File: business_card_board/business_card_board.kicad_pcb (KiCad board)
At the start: 2 copper layers, 23 parts, among them J1 PICKit3_Programmer, SW1 SW_Push, SW2 SW_Push, U1 PIC12F1822

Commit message: layout almost done
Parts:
- J1: moved to B.Cu
- moved 128 72.2 mm to (67.0, 98.0), turned to 270 degrees
- moved D10 63.2 mm to (99.1, 90.9), turned to 180 degrees
- moved D9 62.5 mm to (99.2, 85.6), turned to 180 degrees
- moved R5 61.5 mm to (101.7, 78.3), turned to 90 degrees
- moved 64 60.9 mm to (73.0, 98.0), turned to 90 degrees
- moved R7 60.3 mm to (93.5, 85.6)
- moved R8 60.1 mm to (93.4, 90.9), turned to 180 degrees
- moved 32 49.7 mm to (79.0, 98.0), turned to 270 degrees
- moved R4 49.4 mm to (105.2, 78.3)
- moved U1 47.6 mm to (107.8, 70.7), turned to 180 degrees
- moved R3 43.3 mm to (108.6, 78.3)
- moved R6 43.2 mm to (112.0, 78.3)
- moved C1 39.4 mm to (111.9, 70.9), turned to 270 degrees
- moved R2 38.4 mm to (102.3, 69.2), turned to 0 degrees
- moved 16 38.4 mm to (85.0, 98.0), turned to 90 degrees
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- renumbered SW2 to ->, D1 to 1, D8 to 128, D5 to 16, D2 to 2, D6 to 32, D3 to 4, D7 to 64, D4 to 8, SW1 to <-
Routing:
- net VPP/~MCLR: track 0.00 -> 93.1 mm, vias 0 -> 1
- net Net-(D1-Pad1): track 0.00 -> 74.2 mm
- net Net-(D5-Pad1): track 0.00 -> 68.5 mm
- net Net-(R1-Pad2): track 0.00 -> 61.5 mm
- net Net-(D3-Pad1): track 0.00 -> 48.2 mm
- net Net-(D1-Pad2): track 0.00 -> 44.9 mm
- net ICSPCLK: track 0.00 -> 21.6 mm, vias 0 -> 1
- net ICSPDAT: track 0.00 -> 20.4 mm, vias 0 -> 1
- net RA5: track 0.00 -> 15.4 mm
- net Net-(R5-Pad2): track 0.00 -> 6.18 mm
- net GND: track 0.00 -> 4.16 mm
- net VCC: track 0.00 -> 3.66 mm
- net Net-(D9-Pad2): track 0.00 -> 3.05 mm
- net Net-(D10-Pad2): track 0.00 -> 3.05 mm
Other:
- board outline added: 85 x 54 mm
- board text added: "0459 590 919"
- board text added: "@_joshajohnson"
- board text added: "Clock Driven"
- board text added: "Josh Johnson"
- board text added: "Single Step"
- board text added: "josh@joshajohnson.com"
- board text added: "joshajohnson.com"

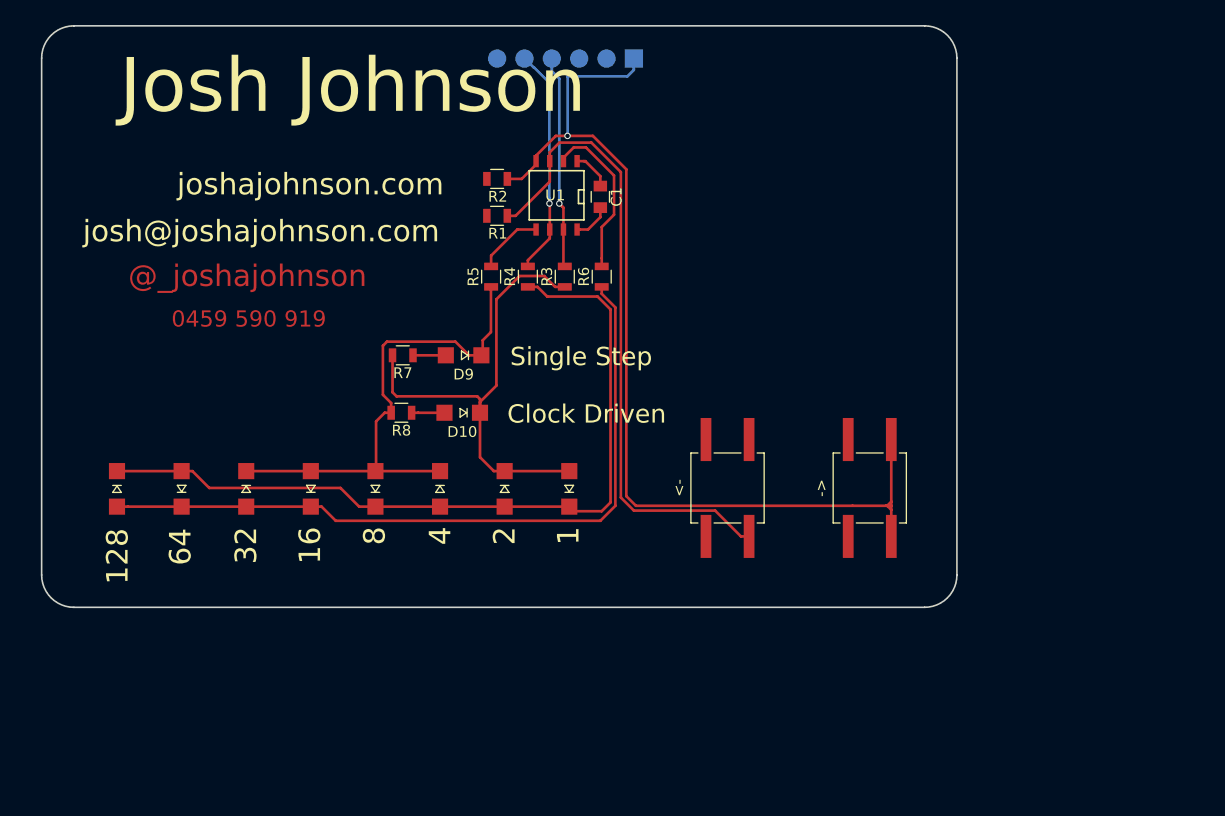
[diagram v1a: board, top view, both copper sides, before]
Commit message: CR2032 Holder added + everything connected
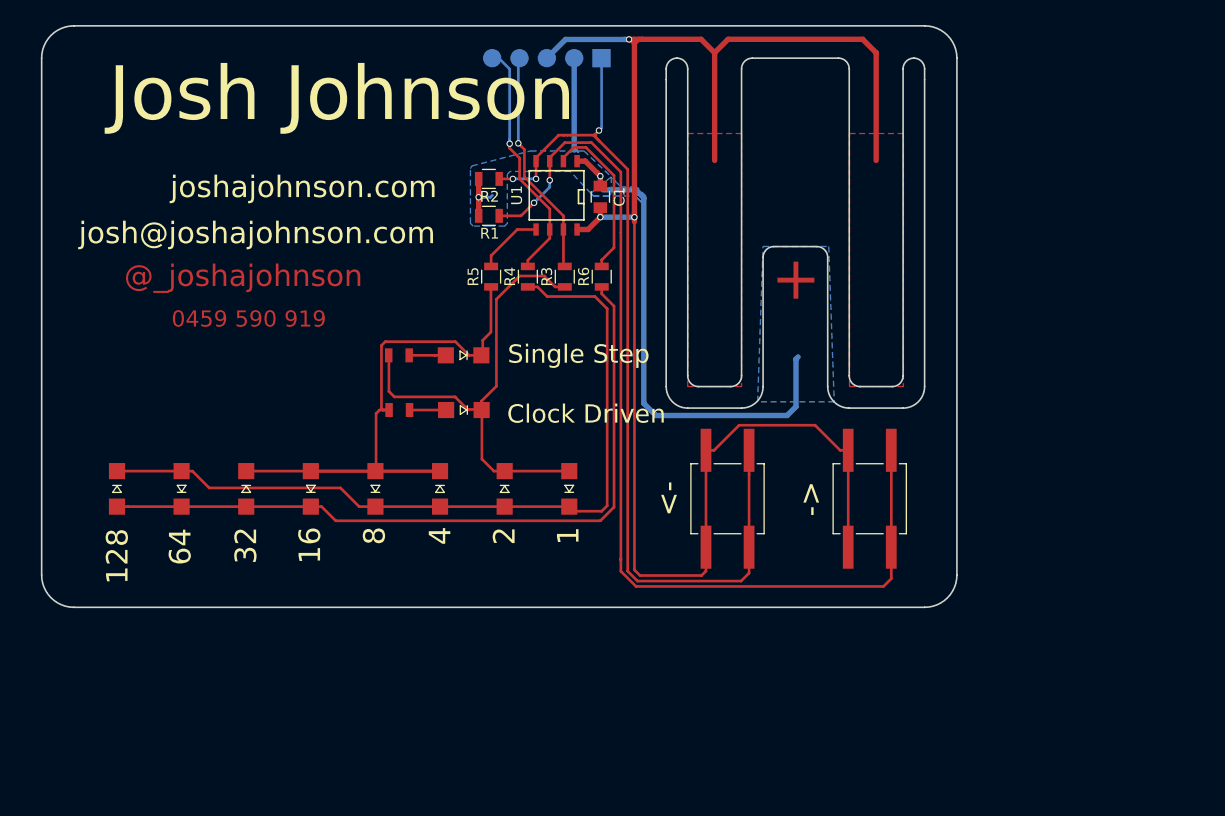
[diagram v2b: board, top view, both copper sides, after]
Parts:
- ?: renamed from R7; footprint Resistors_SMD:R_0805 -> business_card_footprints:R_0805_No_Silk
- ?: renamed from R8; footprint Resistors_SMD:R_0805 -> business_card_footprints:R_0805_No_Silk
- moved J1 3.00 mm to (112.0, 58.0)
- moved -> 1.00 mm to (136.9, 98.9)
- moved <- 1.00 mm to (123.7, 98.9)
- moved R2 0.76 mm to (101.5, 69.2)
- moved R1 0.76 mm to (101.5, 72.6)
- moved ? 0.36 mm to (93.2, 85.6)
- moved ? 0.32 mm to (93.2, 90.7)
- moved ? 0.30 mm to (99.2, 90.7)
- renumbered D10 to ?, D9 to ?
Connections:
- -> pad 2: VPP/~MCLR -> Net-(R1-Pad2)
- <- pad 2: Net-(R1-Pad2) -> VPP/~MCLR
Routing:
- net GND: track 4.16 -> 153.6 mm, vias 0 -> 3
- net VCC: track 3.66 -> 62.4 mm, vias 0 -> 2
- net Net-(R1-Pad2): track 61.5 -> 91.7 mm, vias 0 -> 2
- net Net-(D3-Pad1): track 48.2 -> 60.4 mm
- net VPP/~MCLR: track 93.1 -> 85.1 mm, vias 1 -> 3
- net ICSPDAT: track 20.4 -> 21.7 mm
- net ICSPCLK: track 21.6 -> 22.8 mm
- net Net-(D1-Pad2): track 44.9 -> 44.3 mm
- added copper zone on F.Cu, net GND
- added copper zone on B.Cu, net VCC
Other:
- outline, holes or cut-outs redrawn
- board text added: "+"

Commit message: minor routing changes + test bit output code
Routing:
- net GND: track 153.6 -> 155.6 mm
- net VCC: track 62.4 -> 63.4 mm
- net Net-(D3-Pad1): track 60.4 -> 61.0 mm
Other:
- board text added: "-"
- board text added: "github.com/joshajohnson/Business_Card"

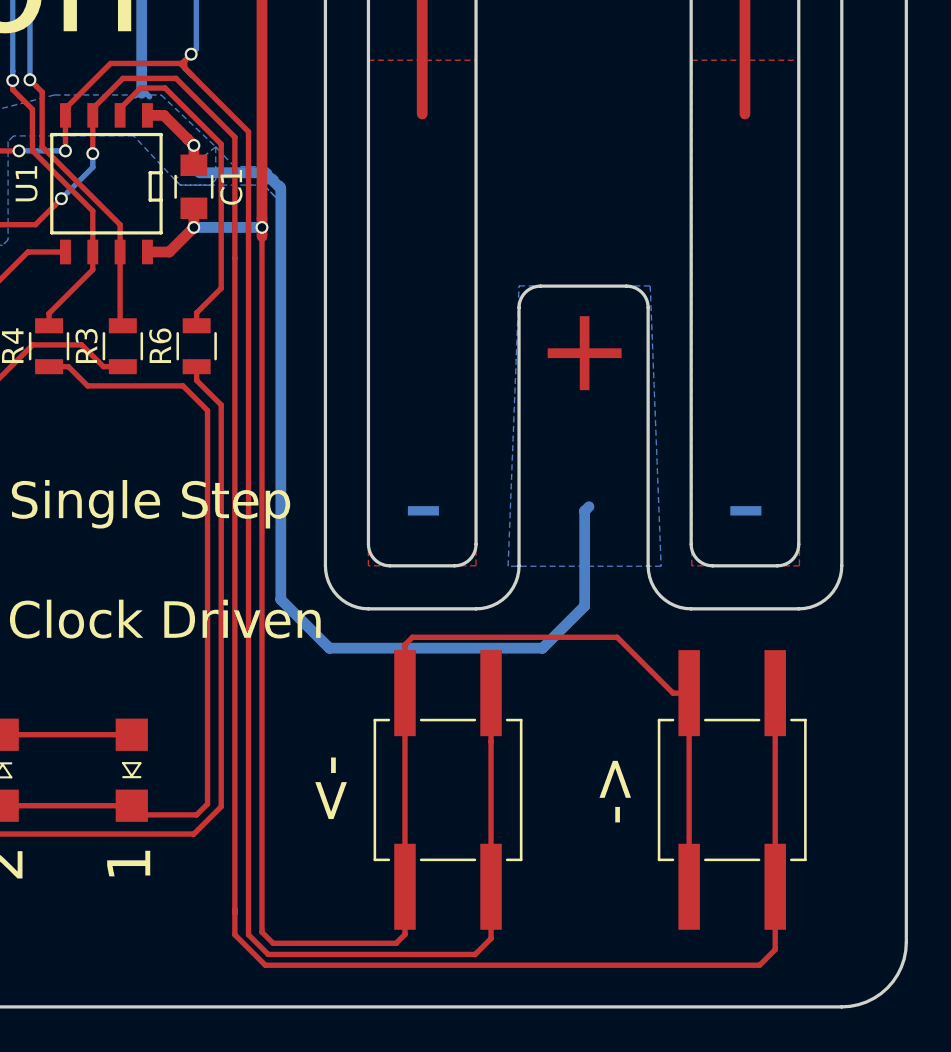
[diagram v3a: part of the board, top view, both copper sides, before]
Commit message: gerbers sent to fab, small change to trace on d1 after files sent.
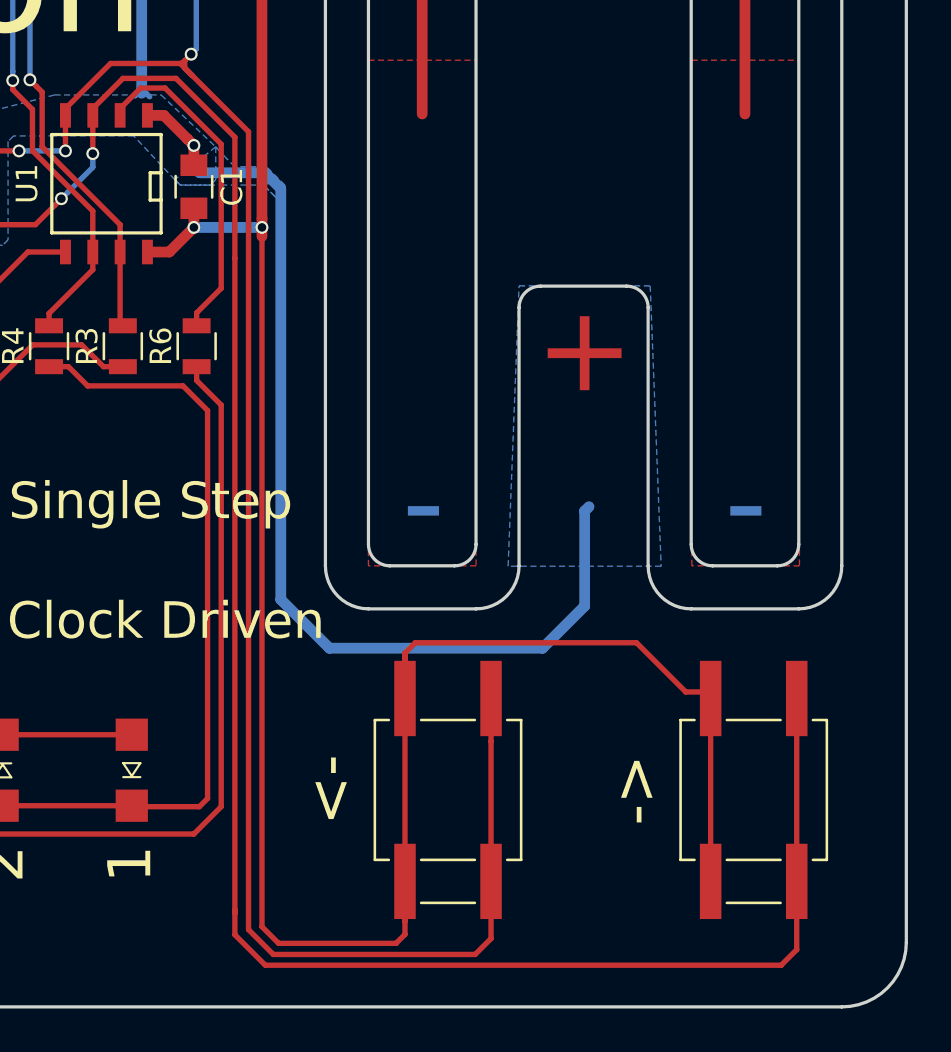
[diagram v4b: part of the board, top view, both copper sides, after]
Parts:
- moved -> 1.00 mm to (137.9, 98.9)
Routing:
- net GND: track 155.6 -> 159.9 mm
- net Net-(R1-Pad2): track 91.7 -> 92.7 mm

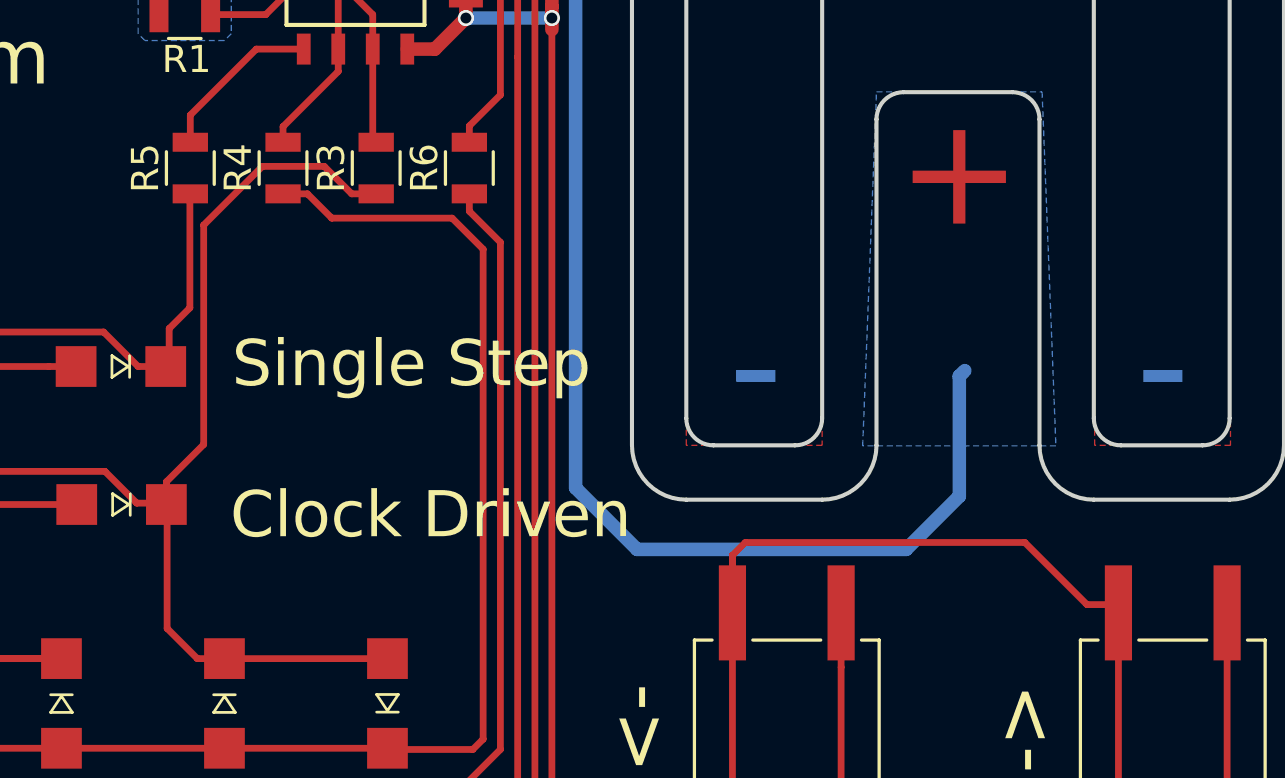
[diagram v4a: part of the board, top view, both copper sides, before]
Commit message: small trace change on right button
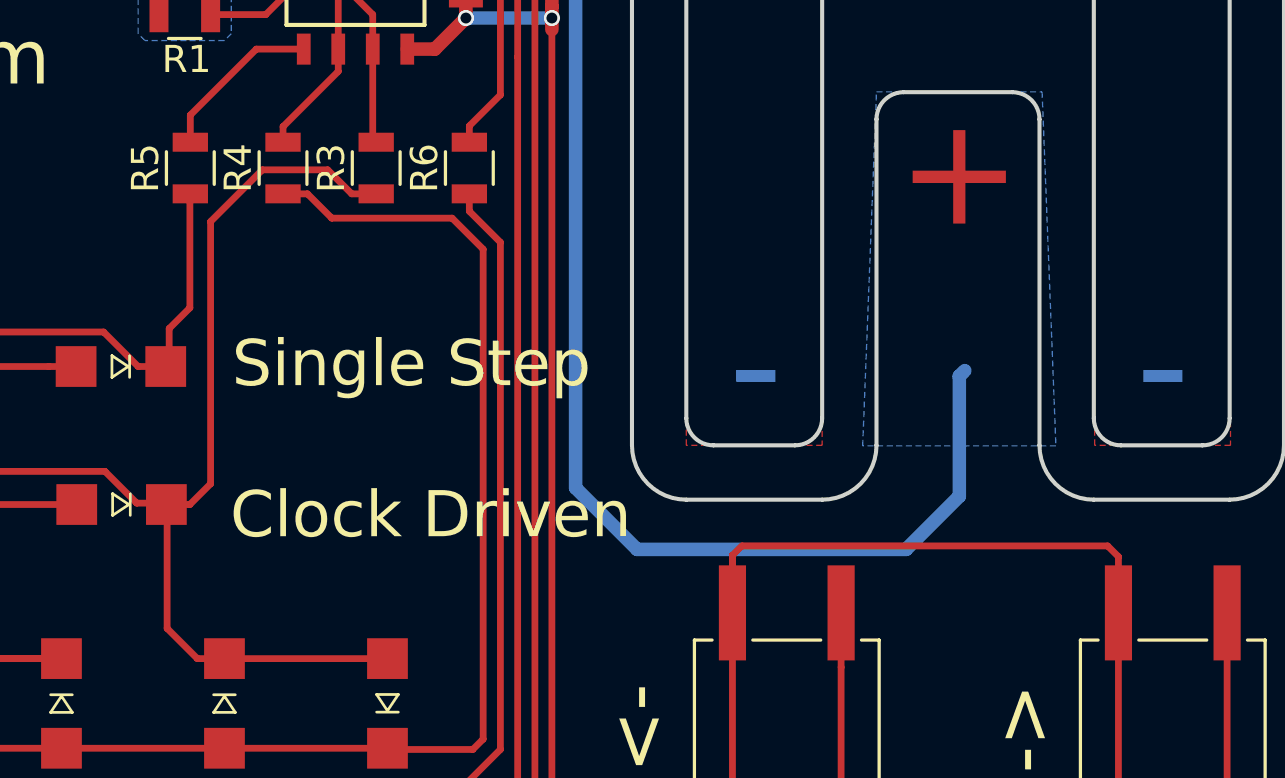
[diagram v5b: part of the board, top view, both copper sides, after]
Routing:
- net GND: track 159.9 -> 161.0 mm
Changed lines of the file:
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@@
     (thickness 1.6)
     (drawings 53)
-    (tracks 235)
+    (tracks 234)
     (zones 0)
     (modules 23)
@@
   (segment (start 110.49 67.564) (end 110.363 67.564) (width 0.25) (layer F.Cu) (net 1))
   (segment (start 110.363 67.564) (end 109.728 67.564) (width 0.5) (layer F.Cu) (net 1))
-  (segment (start 121.698 92.551) (end 122.174 92.075) (width 0.25) (layer F.Cu) (net 2))
-  (segment (start 132.461 92.075) (end 134.747 94.361) (width 0.25) (layer F.Cu) (net 2))
-  (segment (start 122.174 92.075) (end 132.461 92.075) (width 0.25) (layer F.Cu) (net 2))
-  (segment (start 134.747 94.361) (end 135.636 94.361) (width 0.25) (layer F.Cu) (net 2))
-  (segment (start 135.636 94.361) (end 135.906 94.631) (width 0.25) (layer F.Cu) (net 2))
+  (segment (start 121.698 92.551) (end 122.047 92.202) (width 0.25) (layer F.Cu) (net 2))
+  (segment (start 122.047 92.202) (end 135.509 92.202) (width 0.25) (layer F.Cu) (net 2))
+  (segment (start 135.509 92.202) (end 135.906 92.599) (width 0.25) (layer F.Cu) (net 2))
+  (segment (start 135.906 92.599) (end 135.906 94.631) (width 0.25) (layer F.Cu) (net 2))
   (segment (start 135.906 94.631) (end 135.906 103.417) (width 0.25) (layer F.Cu) (net 2))
   (segment (start 121.698 92.551) (end 121.698 94.667) (width 0.25) (layer F.Cu) (net 2))
@@
   (segment (start 112.268 72.136) (end 112.268 71.723) (width 0.25) (layer F.Cu) (net 2))
   (segment (start 109.952 73.914) (end 109.728 73.914) (width 0.25) (layer F.Cu) (net 2))
+  (segment (start 108.585 79.243) (end 107.685 79.243) (width 0.25) (layer F.Cu) (net 3))
+  (segment (start 107.685 79.243) (end 106.801 78.359) (width 0.25) (layer F.Cu) (net 3))
+  (segment (start 106.801 78.359) (end 104.394 78.359) (width 0.25) (layer F.Cu) (net 3))
+  (segment (start 104.394 78.359) (end 102.489 80.264) (width 0.25) (layer F.Cu) (net 3))
+  (segment (start 102.489 80.264) (end 102.489 89.916) (width 0.25) (layer F.Cu) (net 3))
+  (segment (start 102.489 89.916) (end 101.727 90.678) (width 0.25) (layer F.Cu) (net 3))
+  (segment (start 101.727 90.678) (end 100.8624 90.678) (width 0.25) (layer F.Cu) (net 3))
   (segment (start 92.2528 85.5472) (end 92.2528 88.9508) (width 0.25) (layer F.Cu) (net 3))
   (segment (start 92.2528 88.9508) (end 92.7608 89.4588) (width 0.25) (layer F.Cu) (net 3))
@@
   (segment (start 98.6028 89.4588) (end 99.7712 90.6272) (width 0.25) (layer F.Cu) (net 3))
   (segment (start 99.7712 90.6272) (end 100.9904 90.6272) (width 0.25) (layer F.Cu) (net 3))
-  (segment (start 108.585 79.243) (end 107.685 79.243) (width 0.25) (layer F.Cu) (net 3))
-  (segment (start 107.685 79.243) (end 106.674 78.232) (width 0.25) (layer F.Cu) (net 3))
-  (segment (start 106.674 78.232) (end 104.394 78.232) (width 0.25) (layer F.Cu) (net 3))
-  (segment (start 104.394 78.232) (end 102.235 80.391) (width 0.25) (layer F.Cu) (net 3))
-  (segment (start 102.235 80.391) (end 102.235 88.4682) (width 0.25) (layer F.Cu) (net 3))
-  (segment (start 102.235 88.4682) (end 100.8624 89.8408) (width 0.25) (layer F.Cu) (net 3))
-  (segment (start 100.8624 89.8408) (end 100.8624 90.678) (width 0.25) (layer F.Cu) (net 3))
   (segment (start 100.711 90.932) (end 100.8888 91.1098) (width 0.25) (layer F.Cu) (net 3))
   (segment (start 100.8888 91.1098) (end 100.8888 95.2388) (width 0.25) (layer F.Cu) (net 3))
